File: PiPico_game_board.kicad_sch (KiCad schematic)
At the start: 18 parts, among them U1 Pico

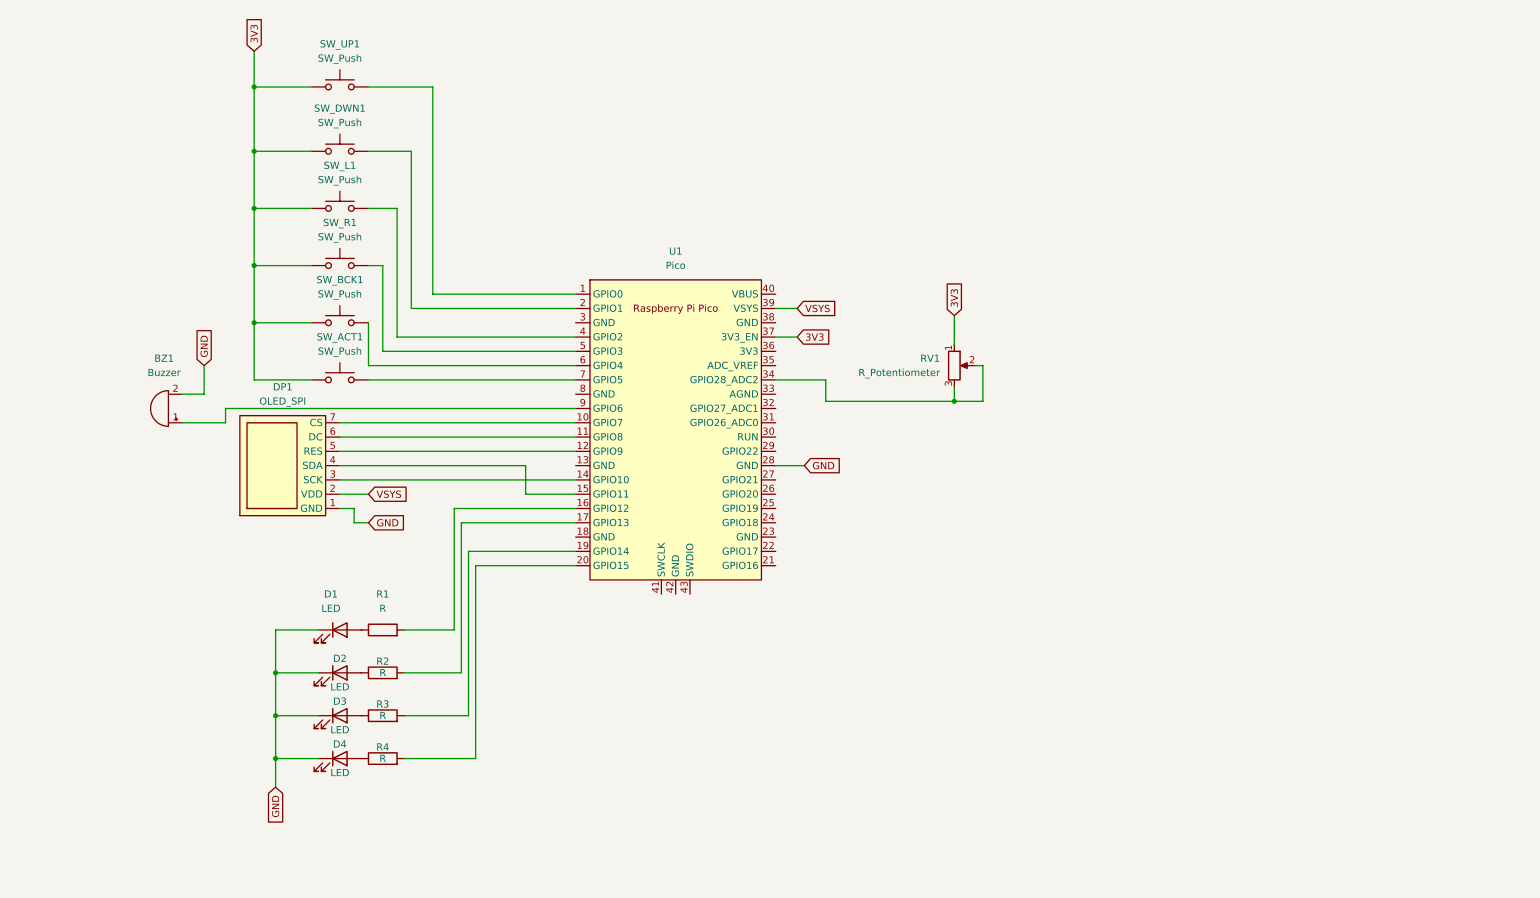
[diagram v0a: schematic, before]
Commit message: Minor schematic changes
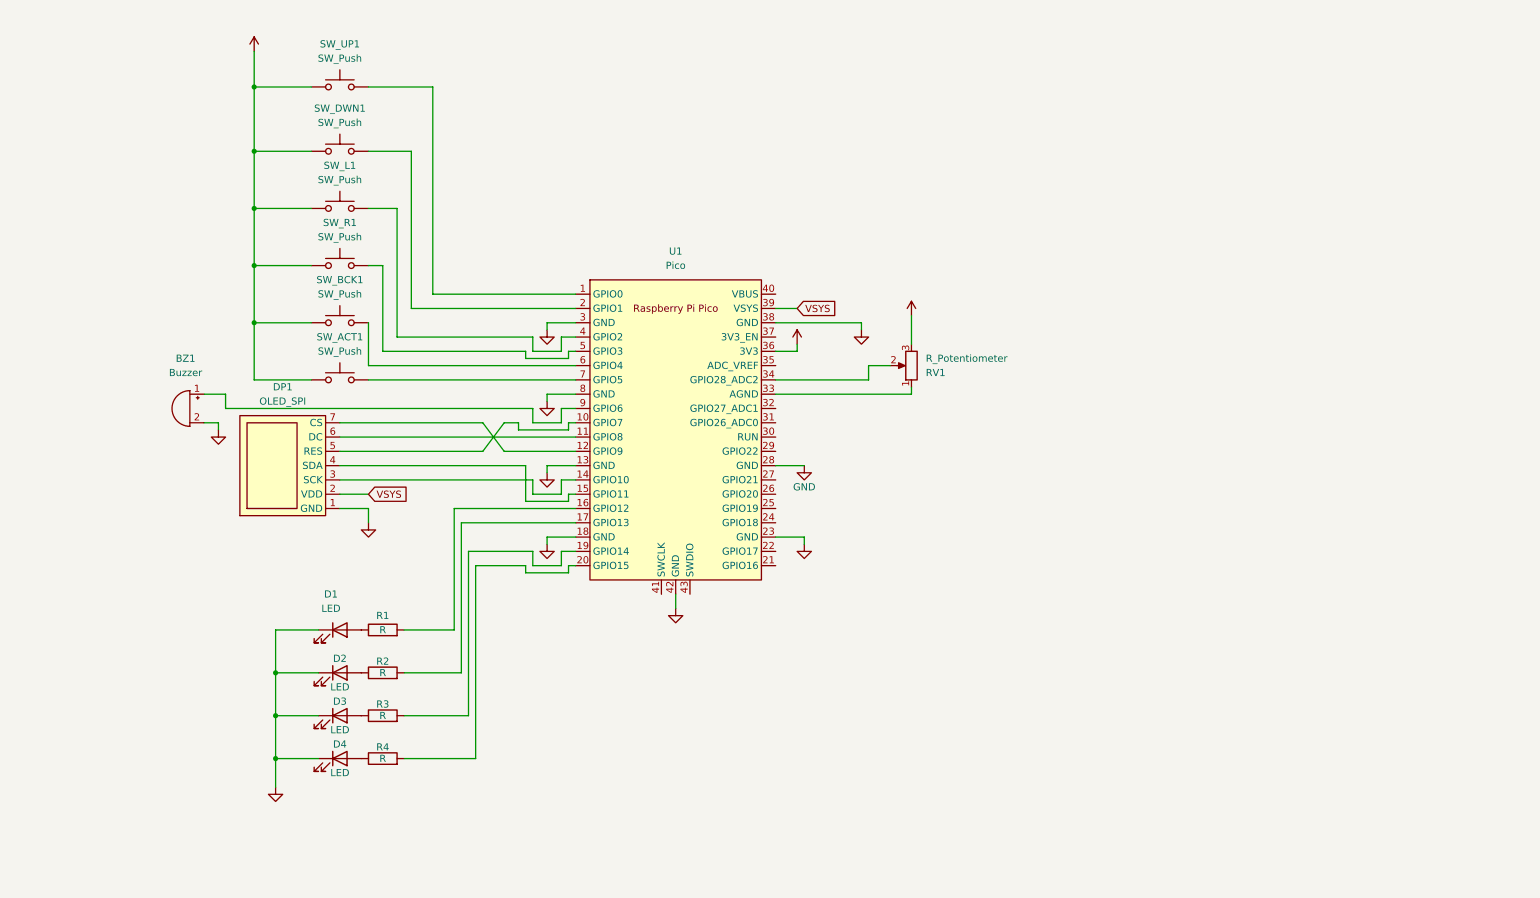
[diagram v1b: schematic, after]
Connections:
- net GND: now also U1.13 (GND), U1.18 (GND), U1.23 (GND), U1.3 (GND), U1.38 (GND), U1.42 (GND), U1.8 (GND)
- net at DP1.5 (RES): now also U1.10 (GPIO7); no longer U1.12 (GPIO9)
- net at DP1.7 (CS): now also U1.12 (GPIO9); no longer U1.10 (GPIO7)
- net at U1.33 (AGND): now also RV1.1
- net at RV1.2, U1.34 (GPIO28_ADC2): no longer RV1.3
- net +3V3: now reaches U1.36 (3V3)
- net +3V3: now also RV1.3, SW_ACT1.1, SW_BCK1.1, SW_DWN1.1, SW_L1.1, SW_R1.1, SW_UP1.1
- removed net 3V3: RV1.1, SW_ACT1.1, SW_BCK1.1, SW_DWN1.1, SW_L1.1, SW_R1.1, SW_UP1.1, U1.37 (3V3_EN)
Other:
- moved on the sheet: BZ1, RV1

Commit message: External power + pcb change
 - external power source
 - mounting holes
 - buttons position changed
 - changed power for OLED from VSYS to 3V3
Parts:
- added BT1: (no value), symbol Device:Battery
- added D1: (no value), symbol Device:D_Schottky
- added H1, H2, H3, H4: (no value), symbol Mechanical:MountingHole
- DP1: footprint (none) -> _Easy Solder:OLED_Display_Module
- SW_DWN1, SW_L1, SW_R1, SW_UP1: footprint Button_Switch_THT:SW_PUSH_6mm -> _Easy Solder:SW_PUSH-12mm_Omron_Back
- renumbered D2 to D_DWN1, D3 to D_L1, D4 to D_R1, D1 to D_UP1
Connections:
- net +3V3: now also DP1.2 (VDD)
- net GND: now also BT1.2 (-)
- net VSYS: now also D1.1 (K); no longer DP1.2 (VDD)
- net at R4.2: now also U1.21 (GPIO16); no longer U1.20 (GPIO15)
- net at U1.16 (GPIO12): no longer R1.2
- net at U1.17 (GPIO13): no longer R2.2
- net at U1.19 (GPIO14): no longer R3.2
- net at U1.22 (GPIO17): now also R3.2
- net at U1.24 (GPIO18): now also R2.2
- net at U1.25 (GPIO19): now also R1.2
- new net: BT1.1 (+), D1.2 (A)
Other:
- moved on the sheet: D_DWN1, D_L1, D_R1, D_UP1, R1, R2, R3, R4

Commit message: update
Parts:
- added J1: Conn_01x08, Connector_PinHeader_2.54mm:PinHeader_1x08_P2.54mm_Vertical, symbol Connector_Generic:Conn_01x08
- BT1: value (none) -> Battery; footprint (none) -> _Easy Solder:BatteryWire-0.1sqmm_1x02_P3.6mm_D0.4mm_OD1mm_Relief2x_Back
- D1: value (none) -> D_Schottky; footprint (none) -> _Easy Solder:D_DO-41_SOD81_P7.62mm_Horizontal_Big_Pads_Back
- H1, H2, H3, H4: value (none) -> MountingHole; footprint (none) -> MountingHole:MountingHole_2.2mm_M2
- SW_ACT1, SW_BCK1: footprint Button_Switch_THT:SW_PUSH_6mm -> _Easy Solder:SW_PUSH_6mm_Back
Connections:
- net +3V3: now also RV1.1, J1.8 (Pin_8); no longer RV1.3
- net GND: now also RV1.3, U1.33 (AGND), J1.1 (Pin_1)
- net GP12: now reaches U1.16 (GPIO12)
- net GP12: now also J1.2 (Pin_2)
- net GP13: now reaches U1.17 (GPIO13)
- net GP13: now also J1.3 (Pin_3)
- net GP14: now reaches U1.19 (GPIO14)
- net GP14: now also J1.4 (Pin_4)
- net GP15: now reaches U1.20 (GPIO15)
- net GP15: now also J1.5 (Pin_5)
- net GP26: now reaches U1.31 (GPIO26_ADC0)
- net GP26: now also J1.7 (Pin_7)
- net GP27: now reaches U1.32 (GPIO27_ADC1)
- net GP27: now also J1.6 (Pin_6)
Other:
- moved on the sheet: BT1, D1, RV1

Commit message: Fixed previous problems + support for LCD
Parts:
- added DP2: LCD_DISPLAY_ST7735, _Easy Solder:LCD_Display_1.77_Module, symbol Custom_lib:LCD_DISPLAY_ST7735
- renumbered D_R1 to D_L1, D_L1 to D_R1
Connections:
- net +3V3: now also DP2.2 (VDD), DP2.8 (LEDA)
- net GND: now also DP2.1 (GND)
- net at DP1.3 (SCK), U1.14 (GPIO10): now also DP2.3 (SCK)
- net at DP1.4 (SDA), U1.15 (GPIO11): now also DP2.4 (SDA)
- net at DP1.5 (RES), U1.10 (GPIO7): now also DP2.5 (RES)
- net at DP1.6 (DC), U1.11 (GPIO8): now also DP2.6 (DC)
- net at DP1.7 (CS), U1.12 (GPIO9): now also DP2.7 (CS)
